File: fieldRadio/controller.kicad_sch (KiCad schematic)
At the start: 79 parts, among them J3 Conn_01x04_Female, Q1 MOSFET-NCHANNELBSS138, U2 MIC5219-3.3YM5, Y1 32.768kHz

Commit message: Updating field radio
Continued schematic work on field radio
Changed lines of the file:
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@@
+    (stroke (width 0) (type default))
+  )
+  (wire (pts (xy 143.51 27.305) (xy 157.48 27.305))
     (stroke (width 0) (type default))
   )
@@
   )
   (wire (pts (xy 162.56 110.49) (xy 163.83 110.49))
+    (stroke (width 0) (type default))
+  )
+  (wire (pts (xy 143.51 39.37) (xy 143.51 27.305))
     (stroke (width 0) (type default))
   )
@@
     )
   )
+  (global_label "VDD3.3" (shape bidirectional) (at 157.48 27.305 0) (fields_autoplaced)
+    (effects (font (size 1.27 1.27)) (justify left))
+    (property "Intersheetrefs" "${INTERSHEET_REFS}" (at 167.5764 27.305 0)
+      (effects (font (size 1.27 1.27)) (justify left))
+    )
+  )

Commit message: More schematic dev.
More schematic development
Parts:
- removed C36: 0.1uF, Capacitor_SMD:C_0603_1608Metric, symbol Device:C
- removed R38: 39K, Resistor_SMD:R_0603_1608Metric, symbol main-eagle-import:RESISTOR0603
- removed R47: 1K, Resistor_SMD:R_0603_1608Metric, symbol main-eagle-import:RESISTOR0603
- added R105: 100, Resistor_SMD:R_0603_1608Metric, symbol main-eagle-import:RESISTOR0603
- added RV3: R_Potentiometer, Potentiometer_THT:Potentiometer_Bourns_3386C_Horizontal, symbol Device:R_Potentiometer
- renumbered C25 to C100, C28 to C101, C26 to C102, C27 to C103, C29 to C104, C37 to C105, C9 to C107, C35 to C108, C34 to C109, C10 to C110, C21 to C111, C20 to C112, C11 to C113, C13 to C114, C12 to C115, C19 to C116, C18 to C117, C17 to C118, C16 to C119, C15 to C120, C14 to C121, C30 to C122, C31 to C123, C32 to C124, C33 to C125, C22 to C97, C23 to C98, C24 to C99, Q1 to Q23, R27 to R100, R31 to R101, R28 to R102, R32 to R103, R30 to R104, R39 to R107, R46 to R108, R15 to R109, R7 to R110, R40 to R111, R45 to R112, R16 to R113, R8 to R114, R37 to R115, R48 to R116, R1 to R117, R3 to R118, R6 to R119, R41 to R120, R43 to R121, R35 to R122, R44 to R123, R33 to R124, R42 to R125, R34 to R126, R22 to R127, R14 to R128, R21 to R129, R13 to R130, R36 to R131, R20 to R132, R12 to R133, R19 to R134, R11 to R135, R18 to R136, R10 to R137, R17 to R138, R9 to R139, R23 to R95, R24 to R96, R26 to R97, R25 to R98, R29 to R99, U$1 to U$4, U2 to U9
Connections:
- net GND: now also RV3.3
- net VDD5: now also R105.1, RV3.1
- net SIDEBAND_SEL: now reaches U$4.19 (P5.5/UCB0CLK/TA2CLK)
- new net LCD_A: R105.2
- new net LCD_VO: RV3.2

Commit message: Update Connectors
Changed to PCB mount connectors for back panel
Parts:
- removed J3: Conn_01x04_Female, Connector_PinHeader_2.54mm:PinHeader_1x04_P2.54mm_Vertical, symbol Connector:Conn_01x04_Female
- added J10: Conn_01x04, symbol Connector_Generic:Conn_01x04
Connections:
- net GND: now also J10.2 (Pin_2)
- net VDD3.3: now also J10.1 (Pin_1)
- net at C113.2, R119.1, U$4.2 (RST/NMI/SBWTDIO): now also J10.4 (Pin_4)
- net at U$4.3 (TEST/SBWTCK): now also J10.3 (Pin_3)
- no-connect marks 0 -> 3

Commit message: Clean Up
Schematic clean up in prep for layout
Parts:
- J11: renamed from J10; footprint (none) -> Connector_PinHeader_2.54mm:PinHeader_1x04_P2.54mm_Vertical
- renumbered C97 to C105, C98 to C106, C99 to C107, C100 to C108, C101 to C109, C102 to C110, C103 to C111, C104 to C112, C105 to C113, C107 to C114, C108 to C115, C109 to C116, C110 to C117, C111 to C118, C112 to C119, C113 to C120, C114 to C121, C115 to C122, C116 to C123, C117 to C124, C118 to C125, C119 to C126, C120 to C127, C121 to C128, C122 to C129, C123 to C130, C124 to C131, C125 to C132, Q23 to Q19, R107 to R100, R108 to R101, R109 to R102, R110 to R103, R111 to R104, R112 to R105, R113 to R106, R114 to R107, R115 to R108, R116 to R109, R117 to R110, R118 to R111, R119 to R112, R120 to R113, R121 to R114, R122 to R115, R123 to R116, R124 to R117, R125 to R118, R126 to R119, R127 to R120, R128 to R121, R129 to R122, R130 to R123, R131 to R124, R132 to R125, R133 to R126, R134 to R127, R135 to R128, R136 to R129, R137 to R130, R138 to R131, R139 to R132, R95 to R89, R96 to R90, R97 to R91, R98 to R92, R105 to R93, R99 to R94, R100 to R95, R101 to R96, R102 to R97, R103 to R98, R104 to R99, RV3 to RV2, U9 to U7
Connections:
- no-connect marks 3 -> 2

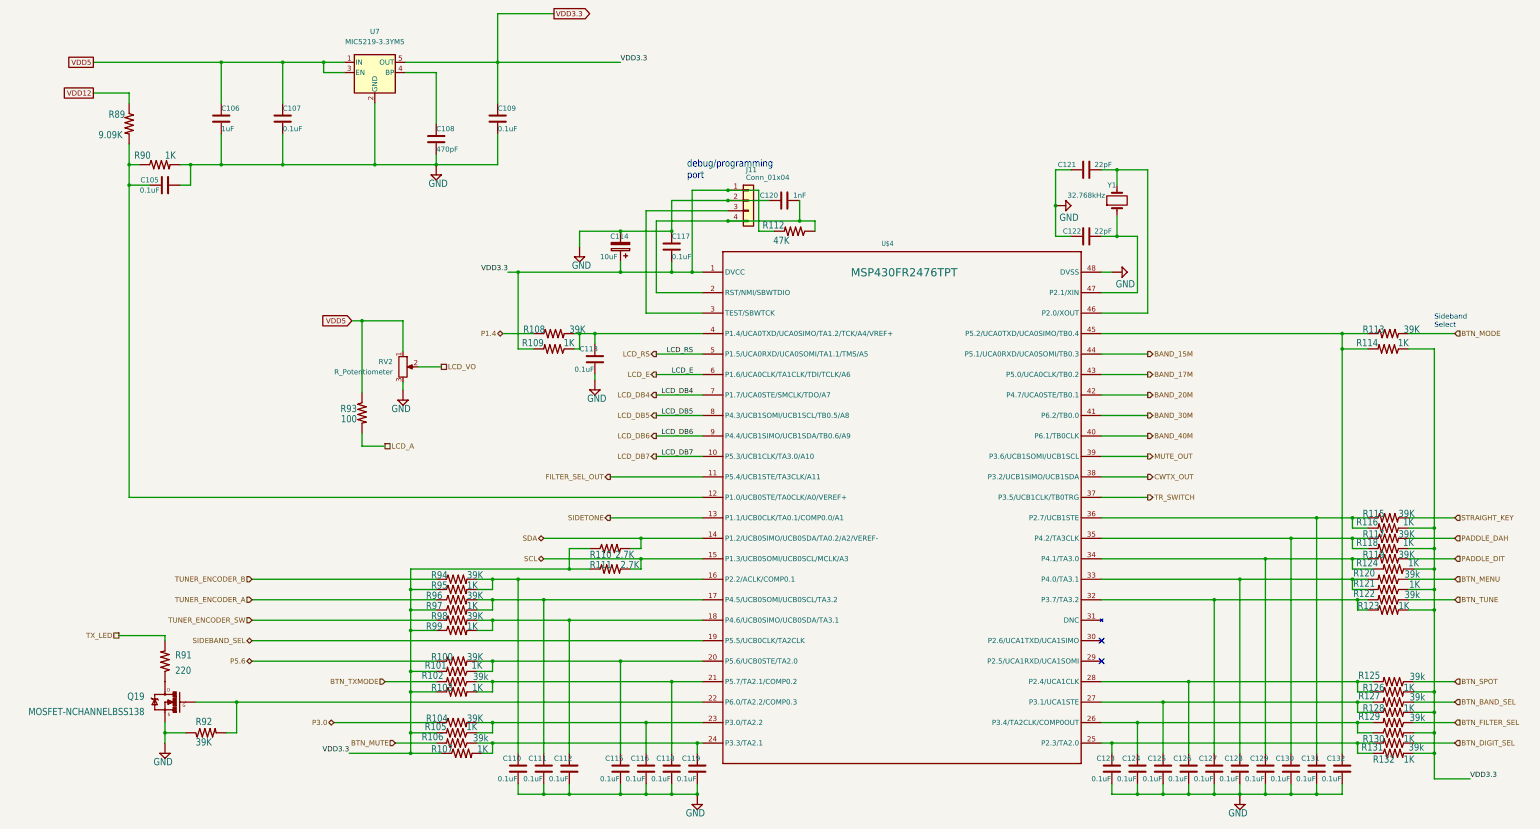
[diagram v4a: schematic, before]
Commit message: Added support for unused gpio
Also added option for external clock generator.
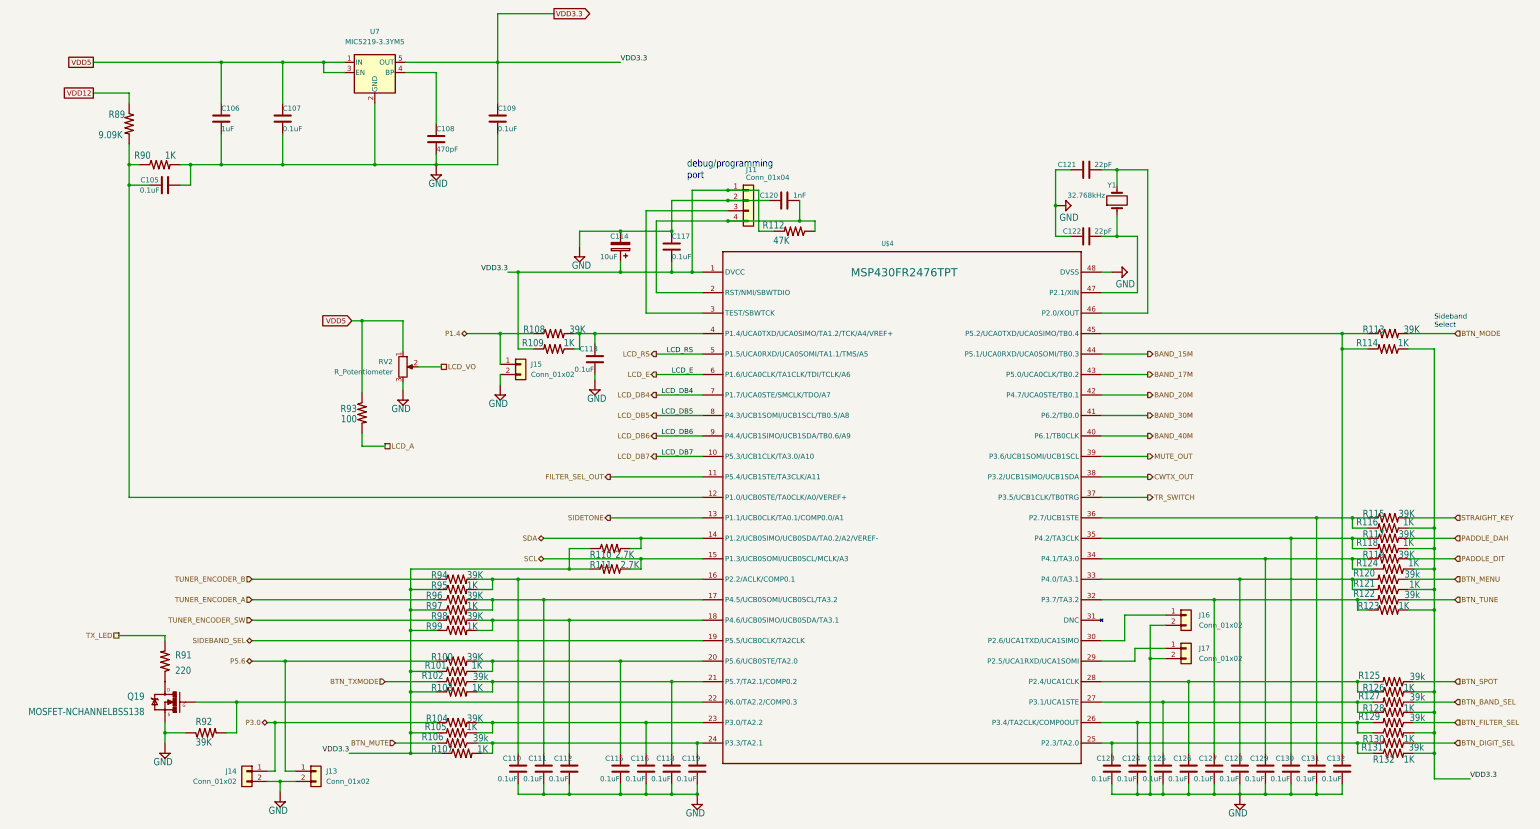
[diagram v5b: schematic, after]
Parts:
- added J13, J14, J15: Conn_01x02, Connector_PinHeader_2.54mm:PinHeader_1x02_P2.54mm_Vertical, symbol Connector_Generic:Conn_01x02
- added J16, J17: Conn_01x02, Connector_PinHeader_2.00mm:PinHeader_1x02_P2.00mm_Vertical, symbol Connector_Generic:Conn_01x02
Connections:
- net GND: now also J13.2 (Pin_2), J14.2 (Pin_2), J15.2 (Pin_2), J16.2 (Pin_2), J17.2 (Pin_2)
- net P1.4: now also J15.1 (Pin_1)
- net P3.0: now also J14.1 (Pin_1)
- net P5.6: now also J13.1 (Pin_1)
- net at U$4.29 (P2.5/UCA1RXD/UCA1SOMI): now also J17.1 (Pin_1)
- net at U$4.30 (P2.6/UCA1TXD/UCA1SIMO): now also J16.1 (Pin_1)
- no-connect marks 2 -> 0

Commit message: finished movement of lcd
Changed lcd connector to move closer to left hand side
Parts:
- C105, C106, C107, C108, C109, C110, C111, C112, C113, C115, C116, C117, C118, C119, C120, C121, C122, C123, C124, C125, C126, C127, C128, C129, C130, C131, C132: footprint Capacitor_SMD:C_0603_1608Metric -> Capacitor_SMD:C_0603_1608Metric_Pad1.08x0.95mm_HandSolder
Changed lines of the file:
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@@
       (effects (font (size 1.27 1.27)) (justify left))
     )
-    (property "Footprint" "Capacitor_SMD:C_0603_1608Metric" (at 129.2352 62.23 0)
+    (property "Footprint" "Capacitor_SMD:C_0603_1608Metric_Pad1.08x0.95mm_HandSolder" (at 129.2352 62.23 0)
       (effects (font (size 1.27 1.27)) hide)
     )
@@
       (effects (font (size 1.27 1.27)) (justify left))
     )
-    (property "Footprint" "Capacitor_SMD:C_0603_1608Metric" (at 181.3052 218.44 0)
+    (property "Footprint" "Capacitor_SMD:C_0603_1608Metric_Pad1.08x0.95mm_HandSolder" (at 181.3052 218.44 0)
       (effects (font (size 1.27 1.27)) hide)
     )
@@
       (effects (font (size 1.27 1.27)) (justify left))
     )
-    (property "Footprint" "Capacitor_SMD:C_0603_1608Metric" (at 162.2552 218.44 0)
+    (property "Footprint" "Capacitor_SMD:C_0603_1608Metric_Pad1.08x0.95mm_HandSolder" (at 162.2552 218.44 0)
       (effects (font (size 1.27 1.27)) hide)
     )
@@
       (effects (font (size 1.27 1.27)) (justify left))
     )
-    (property "Footprint" "Capacitor_SMD:C_0603_1608Metric" (at 354.0252 218.44 0)
+    (property "Footprint" "Capacitor_SMD:C_0603_1608Metric_Pad1.08x0.95mm_HandSolder" (at 354.0252 218.44 0)
       (effects (font (size 1.27 1.27)) hide)
     )
@@
       (effects (font (size 1.27 1.27)) (justify left))
     )
-    (property "Footprint" "Capacitor_SMD:C_0603_1608Metric" (at 293.37 81.5848 0)
+    (property "Footprint" "Capacitor_SMD:C_0603_1608Metric_Pad1.08x0.95mm_HandSolder" (at 293.37 81.5848 0)
       (effects (font (size 1.27 1.27)) hide)
     )
@@
       (effects (font (size 1.27 1.27)) (justify left))
     )
-    (property "Footprint" "Capacitor_SMD:C_0603_1608Metric" (at 341.3252 218.44 0)
+    (property "Footprint" "Capacitor_SMD:C_0603_1608Metric_Pad1.08x0.95mm_HandSolder" (at 341.3252 218.44 0)
       (effects (font (size 1.27 1.27)) hide)
     )
@@
       (effects (font (size 1.27 1.27)) (justify left))
     )
-    (property "Footprint" "Capacitor_SMD:C_0603_1608Metric" (at 296.8752 218.44 0)
+    (property "Footprint" "Capacitor_SMD:C_0603_1608Metric_Pad1.08x0.95mm_HandSolder" (at 296.8752 218.44 0)
       (effects (font (size 1.27 1.27)) hide)
     )
@@
       (effects (font (size 1.27 1.27)) (justify left))
     )
-    (property "Footprint" "Capacitor_SMD:C_0603_1608Metric" (at 144.4752 57.15 0)
+    (property "Footprint" "Capacitor_SMD:C_0603_1608Metric_Pad1.08x0.95mm_HandSolder" (at 144.4752 57.15 0)
       (effects (font (size 1.27 1.27)) hide)
     )
@@
       (effects (font (size 1.27 1.27)))
     )
-    (property "Footprint" "Capacitor_SMD:C_0603_1608Metric" (at 218.44 72.6948 0)
+    (property "Footprint" "Capacitor_SMD:C_0603_1608Metric_Pad1.08x0.95mm_HandSolder" (at 218.44 72.6948 0)
       (effects (font (size 1.27 1.27)) hide)
     )
@@
       (effects (font (size 1.27 1.27)) (justify left))
     )
-    (property "Footprint" "Capacitor_SMD:C_0603_1608Metric" (at 309.5752 218.44 0)
+    (property "Footprint" "Capacitor_SMD:C_0603_1608Metric_Pad1.08x0.95mm_HandSolder" (at 309.5752 218.44 0)
       (effects (font (size 1.27 1.27)) hide)
     )
@@
       (effects (font (size 1.27 1.27)) (justify left))
     )
-    (property "Footprint" "Capacitor_SMD:C_0603_1608Metric" (at 293.37 65.0748 0)
+    (property "Footprint" "Capacitor_SMD:C_0603_1608Metric_Pad1.08x0.95mm_HandSolder" (at 293.37 65.0748 0)
       (effects (font (size 1.27 1.27)) hide)
     )
@@
       (effects (font (size 1.27 1.27)) (justify left))
     )
-    (property "Footprint" "Capacitor_SMD:C_0603_1608Metric" (at 187.6552 88.9 0)
+    (property "Footprint" "Capacitor_SMD:C_0603_1608Metric_Pad1.08x0.95mm_HandSolder" (at 187.6552 88.9 0)
       (effects (font (size 1.27 1.27)) hide)
     )
@@
       (effects (font (size 1.27 1.27)) (justify left))
     )
-    (property "Footprint" "Capacitor_SMD:C_0603_1608Metric" (at 75.8952 57.15 0)
+    (property "Footprint" "Capacitor_SMD:C_0603_1608Metric_Pad1.08x0.95mm_HandSolder" (at 75.8952 57.15 0)
       (effects (font (size 1.27 1.27)) hide)
     )
@@
       (effects (font (size 1.27 1.27)) (justify left))
     )
-    (property "Footprint" "Capacitor_SMD:C_0603_1608Metric" (at 328.6252 218.44 0)
+    (property "Footprint" "Capacitor_SMD:C_0603_1608Metric_Pad1.08x0.95mm_HandSolder" (at 328.6252 218.44 0)
       (effects (font (size 1.27 1.27)) hide)
     )
@@
       (effects (font (size 1.27 1.27)) (justify left))
     )
-    (property "Footprint" "Capacitor_SMD:C_0603_1608Metric" (at 347.6752 218.44 0)
+    (property "Footprint" "Capacitor_SMD:C_0603_1608Metric_Pad1.08x0.95mm_HandSolder" (at 347.6752 218.44 0)
       (effects (font (size 1.27 1.27)) hide)
     )
@@
       (effects (font (size 1.27 1.27)) (justify left))
     )
-    (property "Footprint" "Capacitor_SMD:C_0603_1608Metric" (at 322.2752 218.44 0)
+    (property "Footprint" "Capacitor_SMD:C_0603_1608Metric_Pad1.08x0.95mm_HandSolder" (at 322.2752 218.44 0)
       (effects (font (size 1.27 1.27)) hide)
     )
@@
       (effects (font (size 1.27 1.27)) (justify left))
     )
-    (property "Footprint" "Capacitor_SMD:C_0603_1608Metric" (at 187.6552 218.44 0)
+    (property "Footprint" "Capacitor_SMD:C_0603_1608Metric_Pad1.08x0.95mm_HandSolder" (at 187.6552 218.44 0)
       (effects (font (size 1.27 1.27)) hide)
     )
@@
       (effects (font (size 1.27 1.27)) (justify left))
     )
-    (property "Footprint" "Capacitor_SMD:C_0603_1608Metric" (at 155.9052 218.44 0)
+    (property "Footprint" "Capacitor_SMD:C_0603_1608Metric_Pad1.08x0.95mm_HandSolder" (at 155.9052 218.44 0)
       (effects (font (size 1.27 1.27)) hide)
     )
@@
       (effects (font (size 1.27 1.27)) (justify left))
     )
-    (property "Footprint" "Capacitor_SMD:C_0603_1608Metric" (at 168.6052 116.84 0)
+    (property "Footprint" "Capacitor_SMD:C_0603_1608Metric_Pad1.08x0.95mm_HandSolder" (at 168.6052 116.84 0)
       (effects (font (size 1.27 1.27)) hide)
     )
@@
       (effects (font (size 1.27 1.27)) (justify left))
     )
-    (property "Footprint" "Capacitor_SMD:C_0603_1608Metric" (at 303.2252 218.44 0)
+    (property "Footprint" "Capacitor_SMD:C_0603_1608Metric_Pad1.08x0.95mm_HandSolder" (at 303.2252 218.44 0)
       (effects (font (size 1.27 1.27)) hide)
     )
@@
       (effects (font (size 1.27 1.27)) (justify left))
     )
-    (property "Footprint" "Capacitor_SMD:C_0603_1608Metric" (at 91.1352 57.15 0)
+    (property "Footprint" "Capacitor_SMD:C_0603_1608Metric_Pad1.08x0.95mm_HandSolder" (at 91.1352 57.15 0)
       (effects (font (size 1.27 1.27)) hide)
     )
@@
       (effects (font (size 1.27 1.27)) (justify left))
     )
-    (property "Footprint" "Capacitor_SMD:C_0603_1608Metric" (at 315.9252 218.44 0)
+    (property "Footprint" "Capacitor_SMD:C_0603_1608Metric_Pad1.08x0.95mm_HandSolder" (at 315.9252 218.44 0)
       (effects (font (size 1.27 1.27)) hide)
     )
@@
       (effects (font (size 1.27 1.27)) (justify left))
     )
-    (property "Footprint" "Capacitor_SMD:C_0603_1608Metric" (at 194.0052 218.44 0)
+    (property "Footprint" "Capacitor_SMD:C_0603_1608Metric_Pad1.08x0.95mm_HandSolder" (at 194.0052 218.44 0)
       (effects (font (size 1.27 1.27)) hide)
     )
@@
       (effects (font (size 1.27 1.27)) (justify left))
     )
-    (property "Footprint" "Capacitor_SMD:C_0603_1608Metric" (at 334.9752 218.44 0)
+    (property "Footprint" "Capacitor_SMD:C_0603_1608Metric_Pad1.08x0.95mm_HandSolder" (at 334.9752 218.44 0)
       (effects (font (size 1.27 1.27)) hide)
     )
@@
       (effects (font (size 1.27 1.27)))
     )
-    (property "Footprint" "Capacitor_SMD:C_0603_1608Metric" (at 64.77 68.8848 0)
+    (property "Footprint" "Capacitor_SMD:C_0603_1608Metric_Pad1.08x0.95mm_HandSolder" (at 64.77 68.8848 0)
       (effects (font (size 1.27 1.27)) hide)
     )
@@
       (effects (font (size 1.27 1.27)) (justify left))
     )
-    (property "Footprint" "Capacitor_SMD:C_0603_1608Metric" (at 149.5552 218.44 0)
+    (property "Footprint" "Capacitor_SMD:C_0603_1608Metric_Pad1.08x0.95mm_HandSolder" (at 149.5552 218.44 0)
       (effects (font (size 1.27 1.27)) hide)
     )
@@
       (effects (font (size 1.27 1.27)) (justify left))
     )
-    (property "Footprint" "Capacitor_SMD:C_0603_1608Metric" (at 174.9552 218.44 0)
-      (effects (font (size 1.27 1.27)) hide)
-    )
+    (property "Footprint" "Capacitor_SMD:C_0603_1608Metric_Pad1.08x0.95mm_HandSolder" (at 174.9552 218.44 0)
+      (effects (font (size 1.27 1.27)) hide)
+    )
